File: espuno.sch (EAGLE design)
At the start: 61 parts, among them IC1 REG1117, J1 ARDUINO_R3_SHIELD, T1 FDN340P, U1 ADS1115IDGST, U2 NCP1117ST50T3G, U4 FT232R, U5 LMV358IDGKR, U6 MCP73831, U7 TPS61200, X1 POWERSUPPLY_DC21MMX

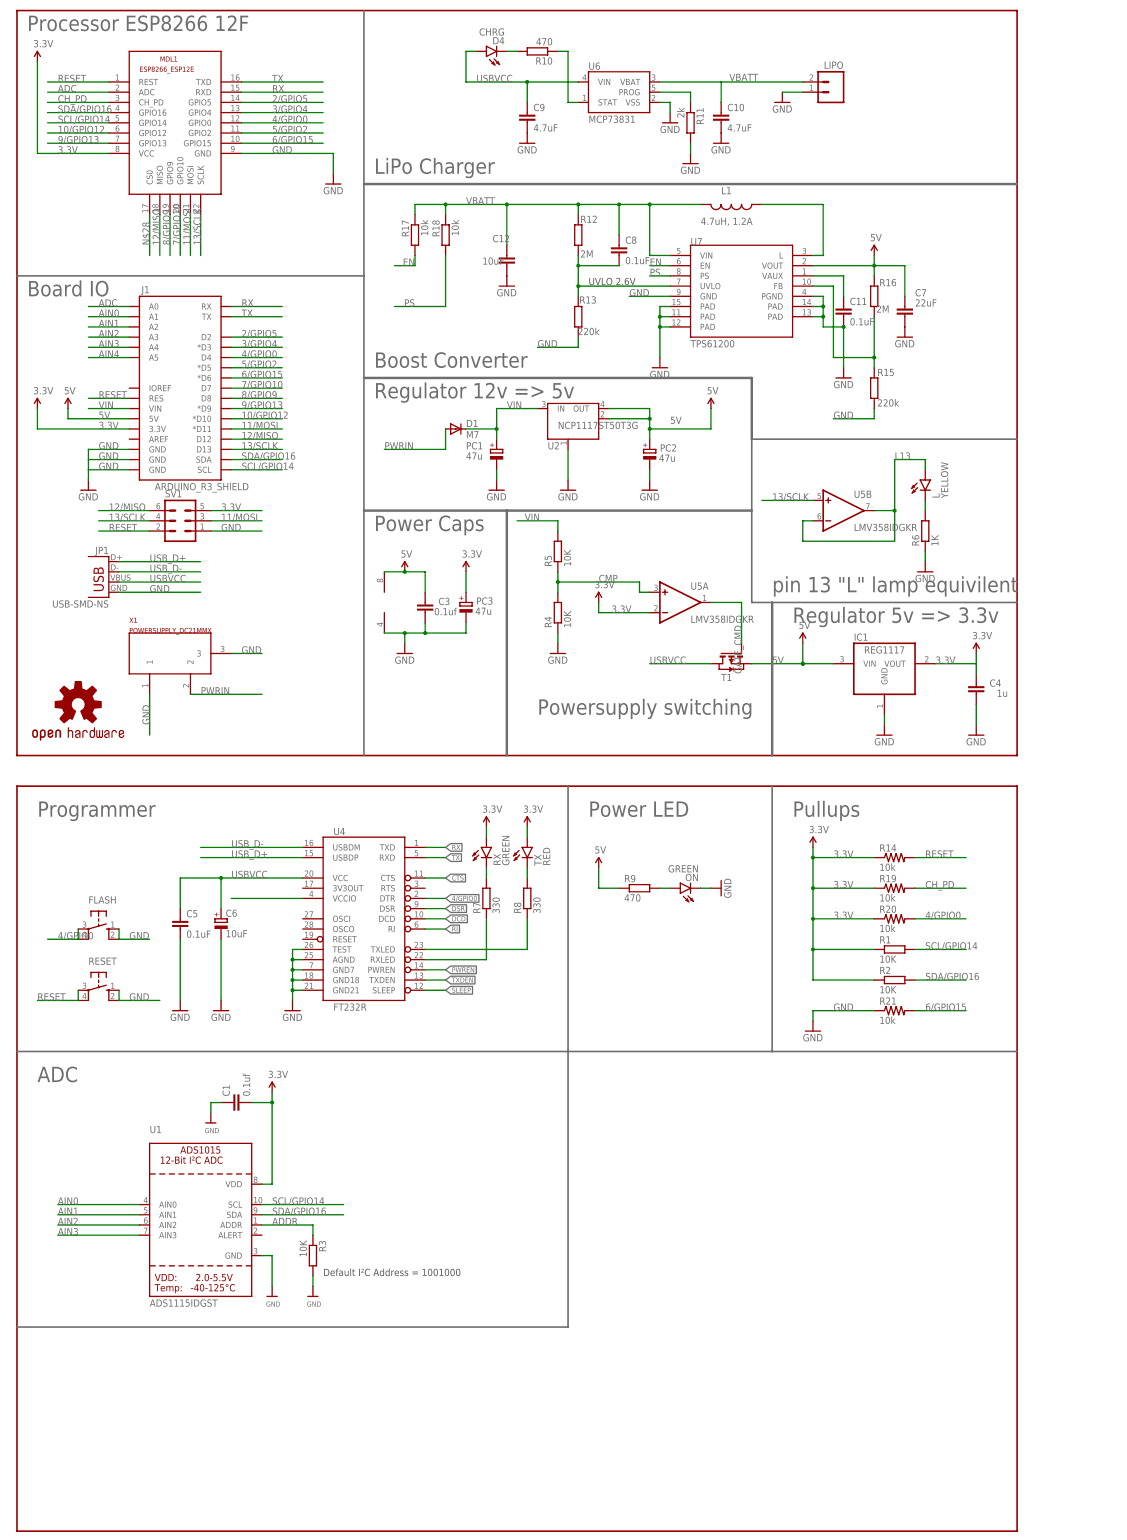
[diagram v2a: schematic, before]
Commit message: Use two ADS1015's and a CAT9531 to interface with the outside world.
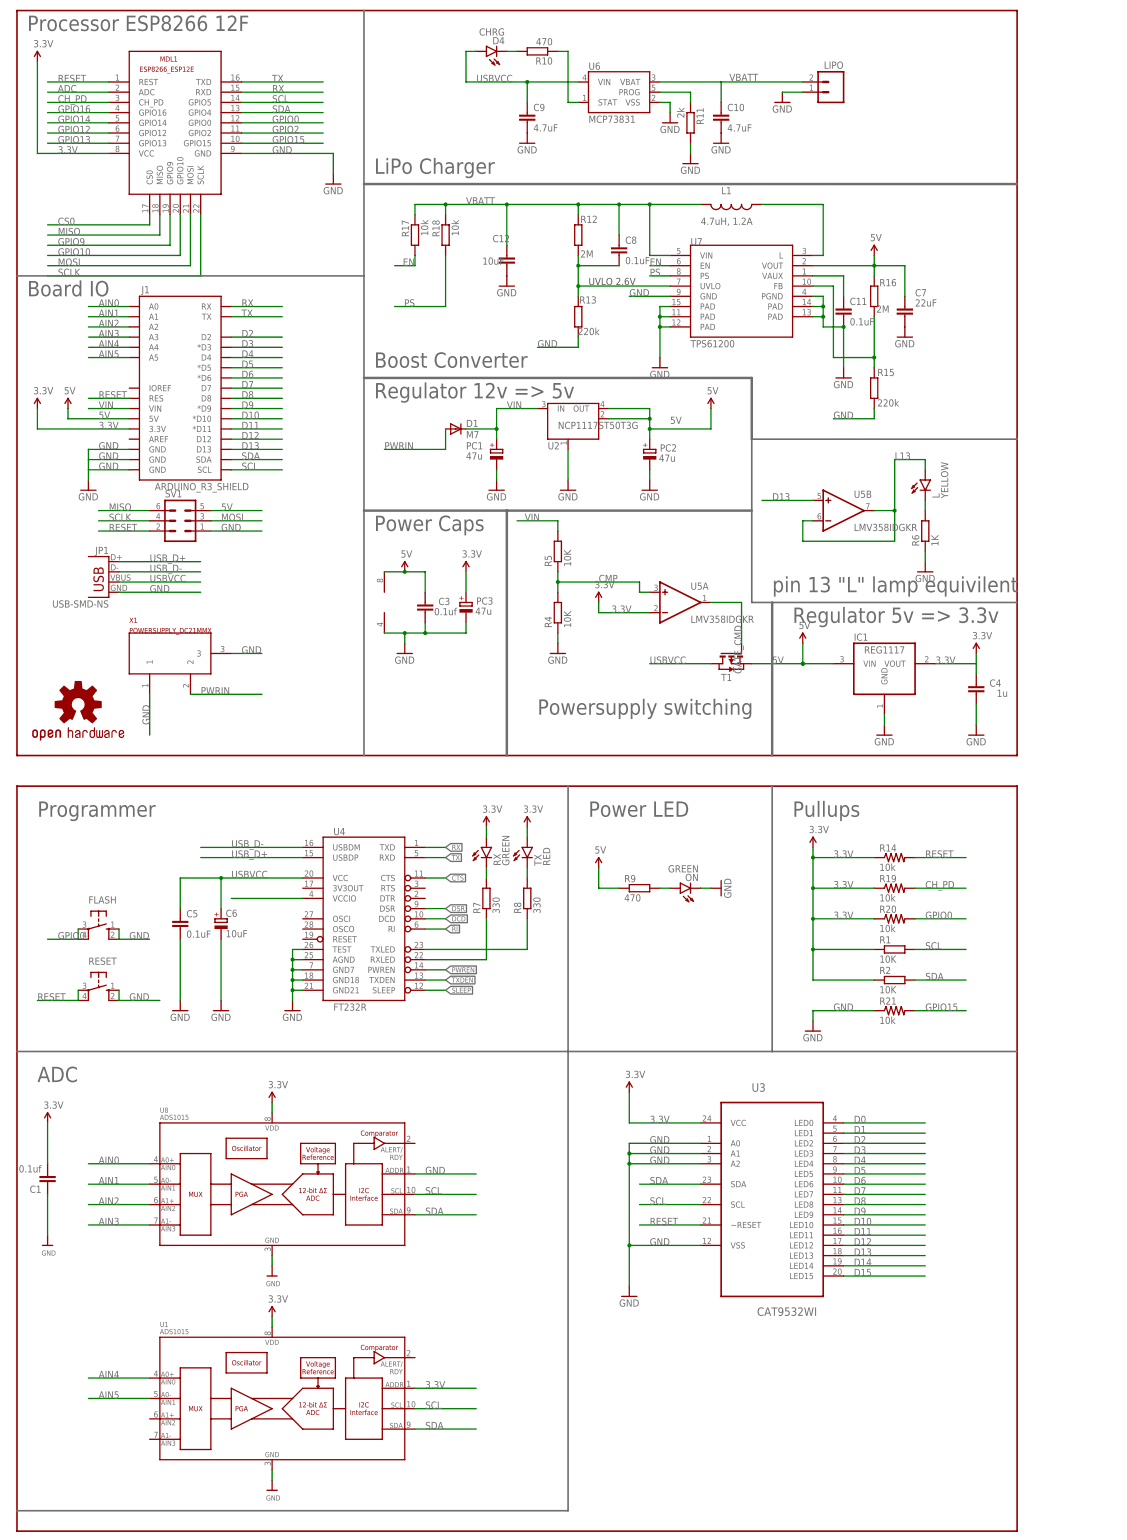
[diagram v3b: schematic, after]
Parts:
- removed R3: 10K, rcl:R-EU_M1206
- added U3: CAT9532WI, ON Semiconductor_By_element14_Batch_1:CAT9532WI
- added U8: ADS1015, SparkFun-AnalogIC:ADS1015
- U1: value ADS1115IDGST -> ADS1015; device microbuilder:ADC_ADS1015 -> SparkFun-AnalogIC:ADS1015
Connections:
- net N$28 renamed CS0
- removed net 10/GPIO12: J1.*D10, MDL1.GPIO12
- removed net 11/MOSI: J1.*D11, MDL1.MOSI, SV1.3
- removed net 12/MISO: J1.D12, MDL1.MISO, SV1.6
- removed net 13/SCLK: J1.D13, MDL1.SCLK, SV1.4, U5B.+IN
- removed net 2/GPIO5: J1.D2, MDL1.GPIO5
- removed net 3/GPIO4: J1.*D3, MDL1.GPIO4
- removed net 4/GPIO0: FLASH.P, FLASH.P1, J1.D4, MDL1.GPIO0, R20.2, U4.DTR
- removed net 5/GPIO2: J1.*D5, MDL1.GPIO2
- removed net 6/GPIO15: J1.*D6, MDL1.GPIO15, R21.2
- removed net 7/GPIO10: J1.D7, MDL1.GPIO10
- removed net 8/GPIO9: J1.D8, MDL1.GPIO9
- removed net 9/GPIO13: J1.*D9, MDL1.GPIO13
- removed net ADDR: R3.1, U1.ADDR
- removed net SCL/GPIO14: J1.SCL, MDL1.GPIO14, R1.2, U1.SCL
- removed net SDA/GPIO16: J1.SDA, MDL1.GPIO16, R2.2, U1.SDA
- new net AIN5: J1.A5, U1.AIN1
- new net D0: U3.LED0
- new net D1: U3.LED1
- new net D10: J1.*D10, U3.LED10
- new net D11: J1.*D11, U3.LED11
- new net D12: J1.D12, U3.LED12
- new net D13: J1.D13, U3.LED13, U5B.+IN
- new net D14: U3.LED14
- new net D15: U3.LED15
- new net D2: J1.D2, U3.LED2
- new net D3: J1.*D3, U3.LED3
- new net D4: J1.D4, U3.LED4
- new net D5: J1.*D5, U3.LED5
- new net D6: J1.*D6, U3.LED6
- new net D7: J1.D7, U3.LED7
- new net D8: J1.D8, U3.LED8
- new net D9: J1.*D9, U3.LED9
- new net GPIO0: FLASH.P, FLASH.P1, MDL1.GPIO0, R20.2
- new net GPIO10: MDL1.GPIO10
- new net GPIO12: MDL1.GPIO12
- new net GPIO13: MDL1.GPIO13
- new net GPIO14: MDL1.GPIO14
- new net GPIO15: MDL1.GPIO15, R21.2
- new net GPIO16: MDL1.GPIO16
- new net GPIO2: MDL1.GPIO2
- new net GPIO9: MDL1.GPIO9
- new net MISO: MDL1.MISO, SV1.6
- new net MOSI: MDL1.MOSI, SV1.3
- new net SCL: J1.SCL, MDL1.GPIO5, R1.2, U1.SCL, U3.SCL, U8.SCL
- new net SCLK: MDL1.SCLK, SV1.4
- new net SDA: J1.SDA, MDL1.GPIO4, R2.2, U1.SDA, U3.SDA, U8.SDA
- net 3.3V: now also U1.ADDR, U3.VCC, U8.VDD; no longer SV1.5
- net 5V: now also SV1.5
- net ADC: no longer J1.A0
- net AIN0: now also J1.A0, U8.AIN0; no longer J1.A1, U1.AIN0
- net AIN1: now also J1.A1, U8.AIN1; no longer J1.A2, U1.AIN1
- net AIN2: now also J1.A2, U8.AIN2; no longer J1.A3, U1.AIN2
- net AIN3: now also J1.A3, U8.AIN3; no longer J1.A4, U1.AIN3
- net AIN4: now also J1.A4, U1.AIN0; no longer J1.A5
- net GND: now also U1.VSS, U3.A0, U3.A1, U3.A2, U3.VSS, U8.ADDR, U8.VSS; no longer R3.2, U1.GND
- net RESET: now also U3.~RESET
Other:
- note removed: "Default I²C Address = 1001000"
- moved on the sheet: C1

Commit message: move adc bits up a bit away from the port
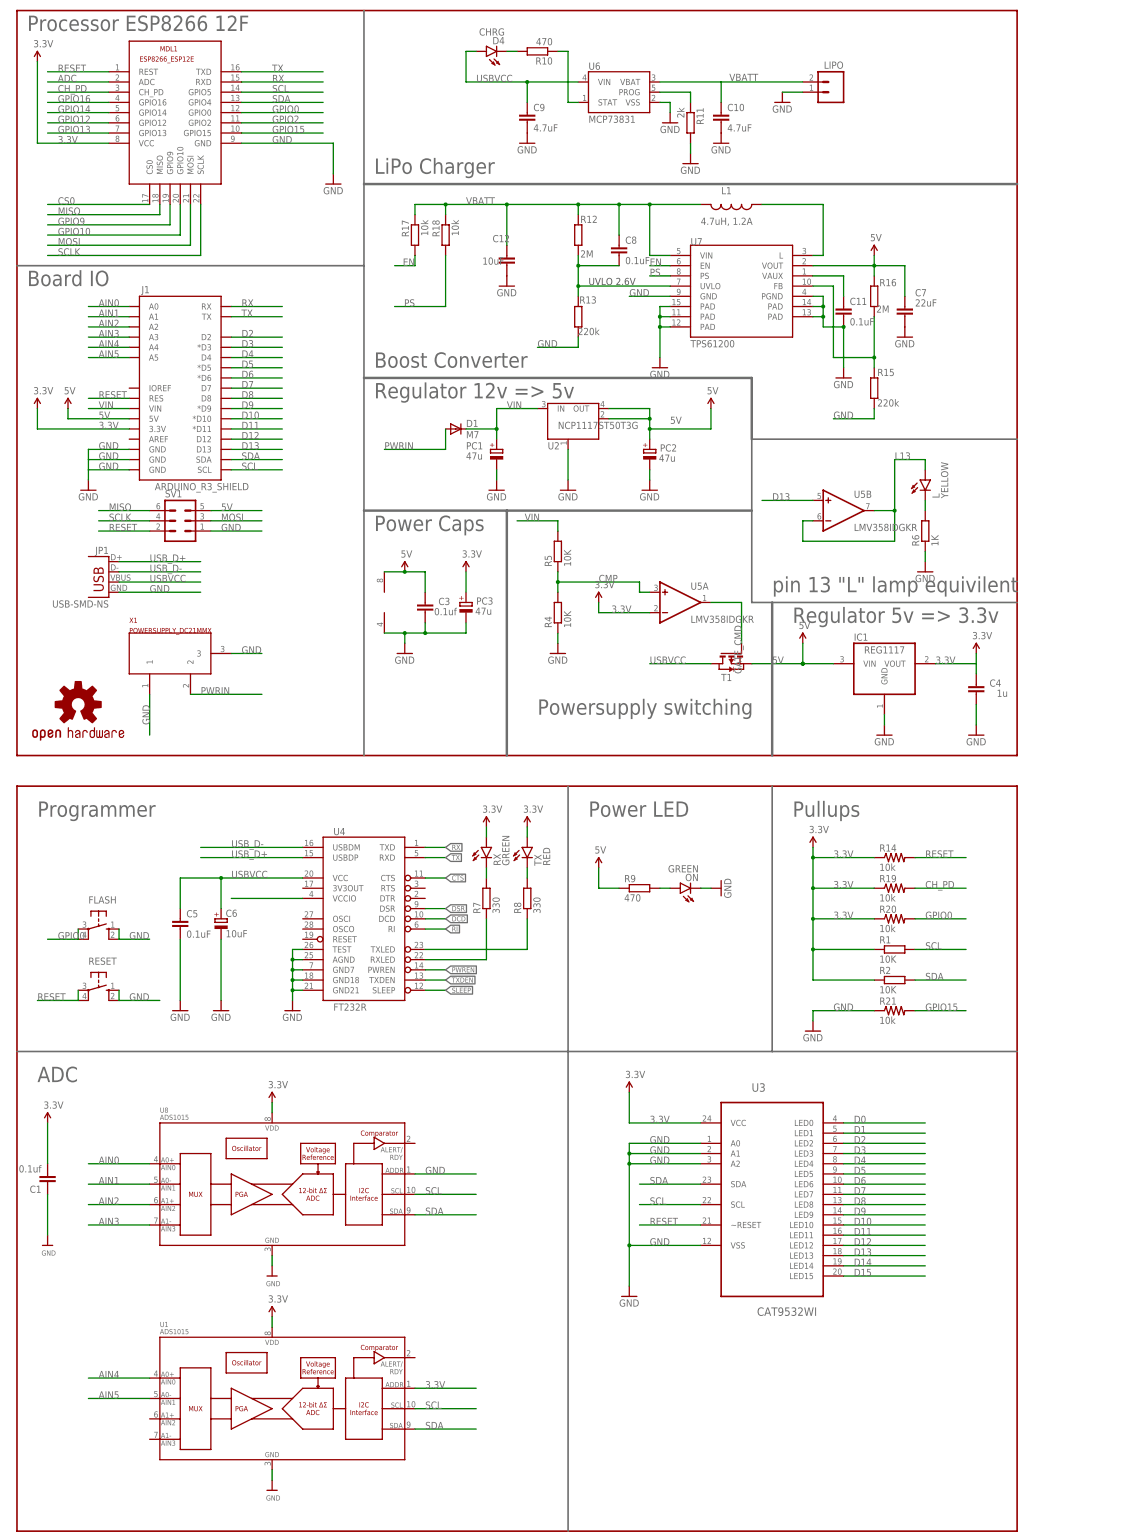
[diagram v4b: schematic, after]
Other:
- moved on the sheet: MDL1

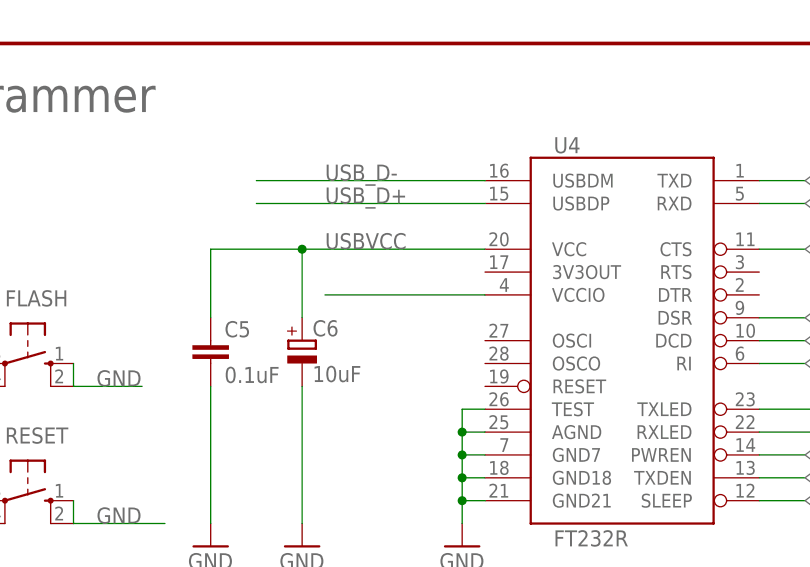
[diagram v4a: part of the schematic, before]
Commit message: Make the FT232R consume its own 3.3v so I can test it by merely attaching USB.
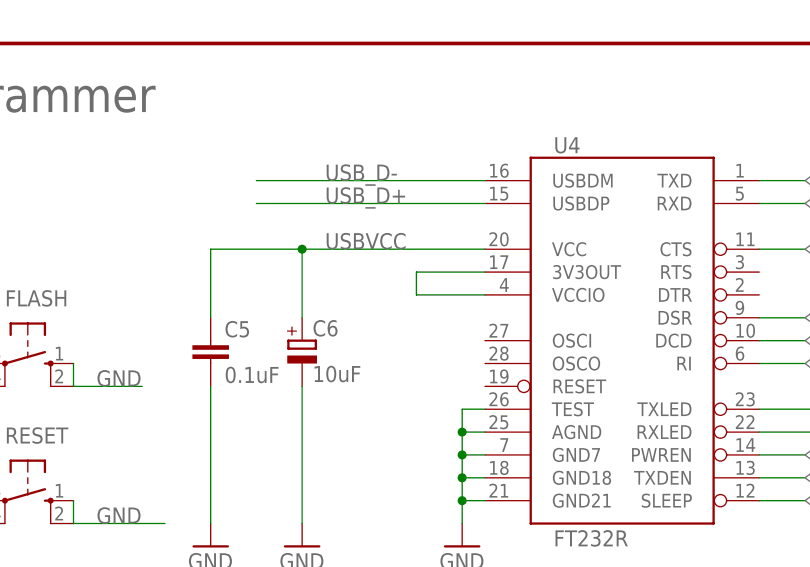
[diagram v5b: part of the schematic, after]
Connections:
- new net N$10: U4.3V3OUT, U4.VCCIO
- net 3.3V: no longer U4.VCCIO
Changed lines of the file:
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@@
-</segment>
-<segment>
-<pinref part="U4" gate="G$1" pin="VCCIO"/>
-<wire x1="71.12" y1="157.48" x2="53.34" y2="157.48" width="0.1524" layer="91"/>
 </segment>
 <segment>
@@
 </segment>
 </net>
+<net name="N$10" class="0">
+<segment>
+<pinref part="U4" gate="G$1" pin="VCCIO"/>
+<wire x1="71.12" y1="157.48" x2="63.5" y2="157.48" width="0.1524" layer="91"/>
+<wire x1="63.5" y1="157.48" x2="63.5" y2="160.02" width="0.1524" layer="91"/>
+<pinref part="U4" gate="G$1" pin="3V3OUT"/>
+<wire x1="63.5" y1="160.02" x2="71.12" y2="160.02" width="0.1524" layer="91"/>
+</segment>
+</net>

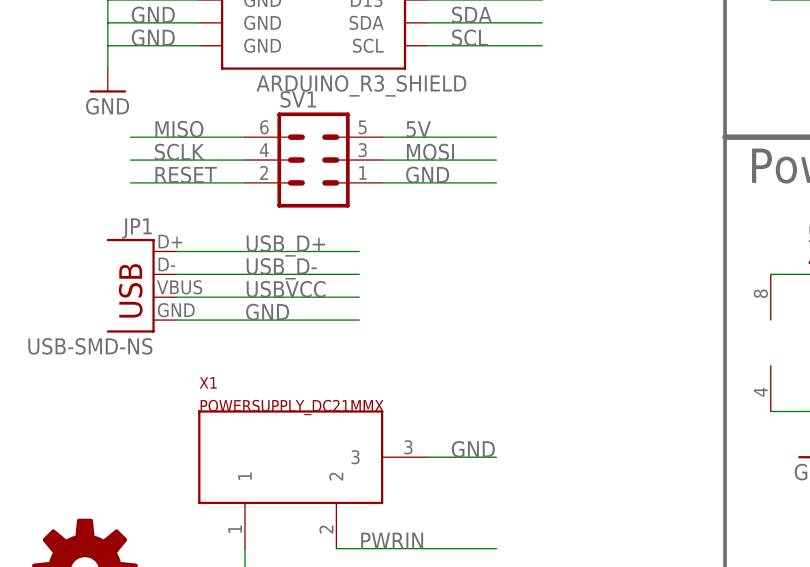
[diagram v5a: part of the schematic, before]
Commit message: Add 500mA fuse
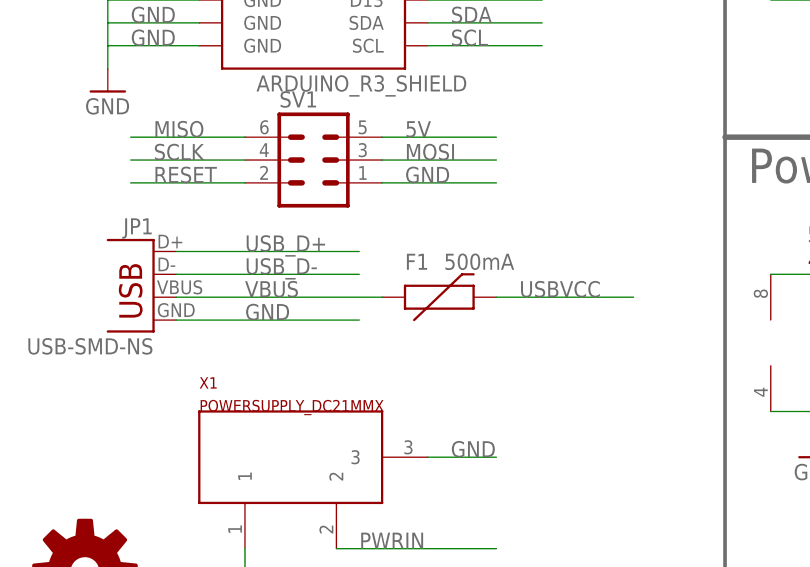
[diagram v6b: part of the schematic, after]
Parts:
- added F1: 500mA, SparkFun:PTCSMD
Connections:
- new net VBUS: F1.1, JP1.VBUS
- net USBVCC: now also F1.2; no longer JP1.VBUS
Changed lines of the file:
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@@
 <part name="U1" library="SparkFun-AnalogIC" deviceset="ADS1015" device="" value="ADS1015"/>
 <part name="U$4" library="microbuilder" deviceset="GND" device=""/>
+<part name="F1" library="SparkFun" deviceset="PTC" device="SMD" value="500mA"/>
 </parts>
 <sheets>
@@
 <instance part="U1" gate="G$1" x="33.02" y="17.78"/>
 <instance part="U$4" gate="G$1" x="63.5" y="10.16"/>
+<instance part="F1" gate="G$1" x="53.34" y="236.22" smashed="yes">
+<attribute name="NAME" x="50.8" y="239.268" size="1.778" layer="95"/>
+<attribute name="VALUE" x="55.118" y="239.268" size="1.778" layer="96"/>
+</instance>
 </instances>
 <busses>
@@
 </segment>
 <segment>
-<wire x1="25.4" y1="236.22" x2="45.72" y2="236.22" width="0.1524" layer="91"/>
-<label x="33.02" y="236.22" size="1.778" layer="95"/>
-<pinref part="JP1" gate="G$1" pin="VBUS"/>
+<pinref part="F1" gate="G$1" pin="2"/>
+<wire x1="60.96" y1="236.22" x2="76.2" y2="236.22" width="0.1524" layer="91"/>
+<label x="63.5" y="236.22" size="1.778" layer="95"/>
 </segment>
 </net>
@@
 </segment>
 </net>
+<net name="VBUS" class="0">
+<segment>
+<wire x1="25.4" y1="236.22" x2="48.26" y2="236.22" width="0.1524" layer="91"/>
+<label x="33.02" y="236.22" size="1.778" layer="95"/>
+<pinref part="JP1" gate="G$1" pin="VBUS"/>
+<pinref part="F1" gate="G$1" pin="1"/>
+</segment>
+</net>
